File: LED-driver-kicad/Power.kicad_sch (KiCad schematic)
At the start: 32 parts, among them U1 LV2862XLVDDCR, U1 PD70210A, U3 LV2862XLVDDCR

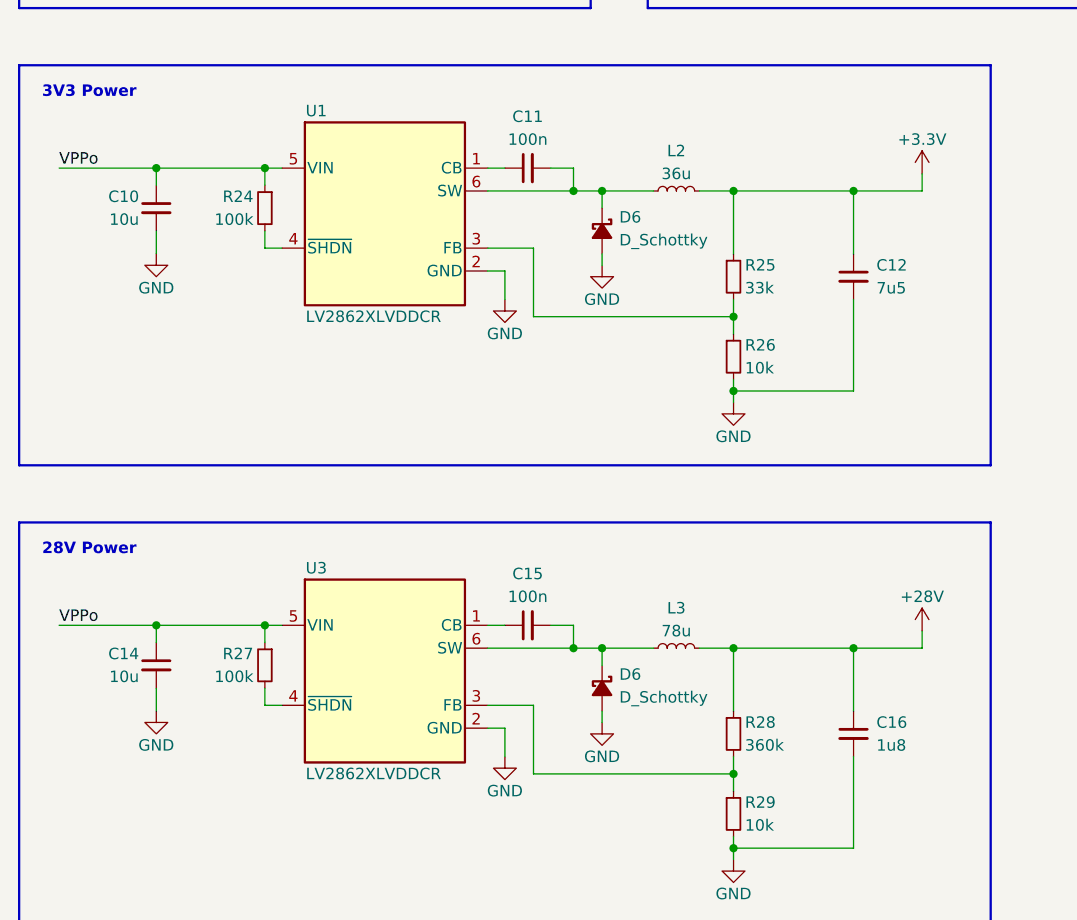
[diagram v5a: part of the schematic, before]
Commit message: update 3V3 power supply circuit
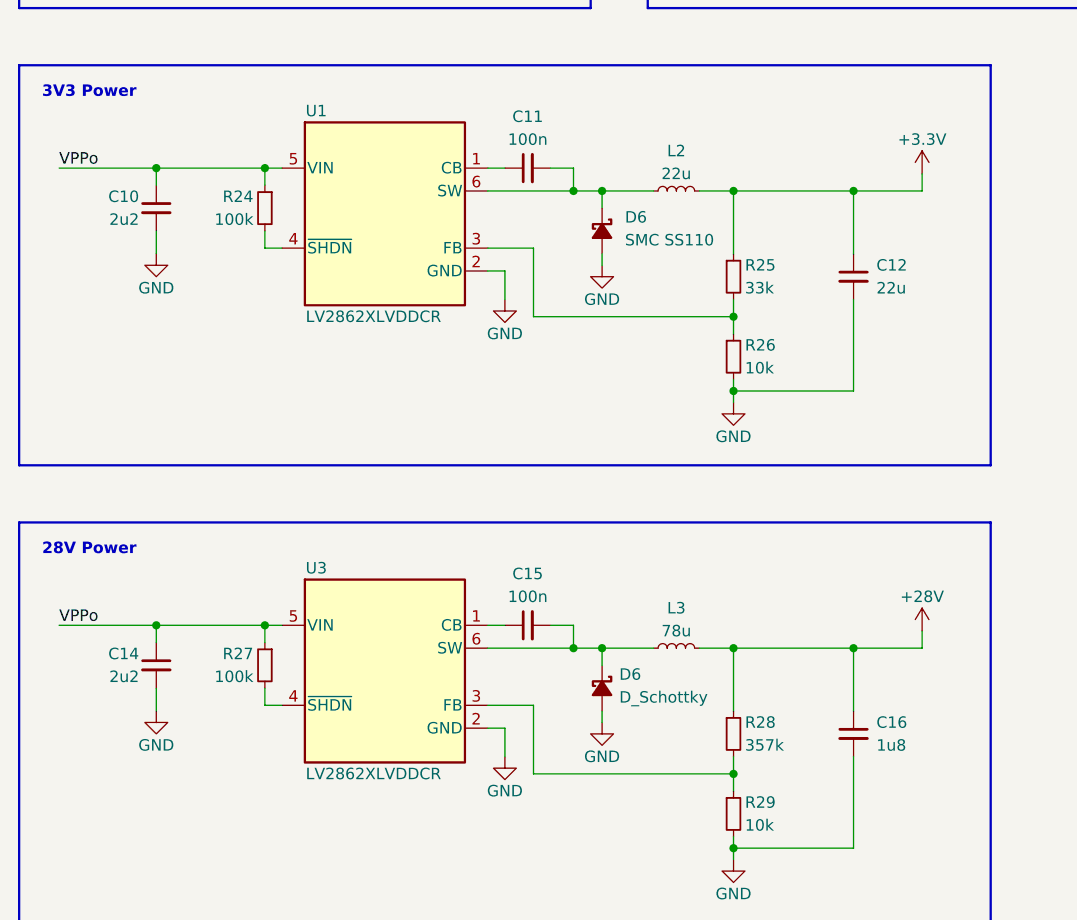
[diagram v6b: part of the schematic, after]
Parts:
- C10, C14: value 10u -> 2u2
- C12: value 7u5 -> 22u
- D6: value D_Schottky -> SMC SS110
- L2: value 36u -> 22u
- R28: value 360k -> 357k
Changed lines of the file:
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@@
       (effects (font (size 1.27 1.27)) (justify left))
     )
-    (property "Value" "7u5" (at 114.3 107.3213 0)
+    (property "Value" "22u" (at 114.3 107.3213 0)
       (effects (font (size 1.27 1.27)) (justify left))
     )
@@
       (effects (font (size 1.27 1.27)) (justify right))
     )
-    (property "Value" "10u" (at 32.385 150.495 0)
+    (property "Value" "2u2" (at 32.385 150.495 0)
       (effects (font (size 1.27 1.27)) (justify right))
     )
@@
   (symbol (lib_id "Device:D_Schottky_Small_Filled") (at 83.82 100.965 270) (unit 1)
     (in_bom yes) (on_board yes) (dnp no) (fields_autoplaced)
-    (property "Reference" "D6" (at 85.725 99.441 90)
-      (effects (font (size 1.27 1.27)) (justify left))
-    )
-    (property "Value" "D_Schottky" (at 85.725 101.981 90)
+    (property "Reference" "D6" (at 86.36 99.441 90)
+      (effects (font (size 1.27 1.27)) (justify left))
+    )
+    (property "Value" "SMC SS110" (at 86.36 101.981 90)
       (effects (font (size 1.27 1.27)) (justify left))
     )
@@
       (effects (font (size 1.27 1.27)))
     )
-    (property "Value" "36u" (at 92.075 94.615 90)
+    (property "Value" "22u" (at 92.075 94.615 90)
       (effects (font (size 1.27 1.27)))
     )
@@
       (effects (font (size 1.27 1.27)) (justify right))
     )
-    (property "Value" "10u" (at 32.385 99.695 0)
+    (property "Value" "2u2" (at 32.385 99.695 0)
       (effects (font (size 1.27 1.27)) (justify right))
     )
@@
       (effects (font (size 1.27 1.27)) (justify left))
     )
-    (property "Value" "360k" (at 99.695 158.115 0)
-      (effects (font (size 1.27 1.27)) (justify left))
-    )
+    (property "Value" "357k" (at 99.695 158.115 0)
+      (effects (font (size 1.27 1.27)) (justify left))
+    )

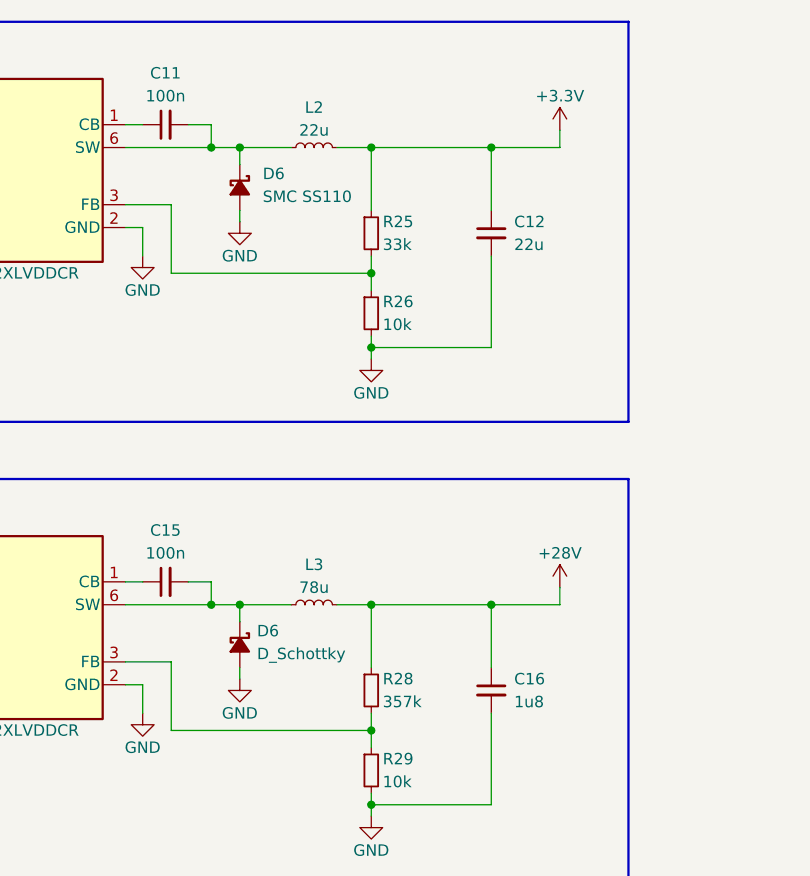
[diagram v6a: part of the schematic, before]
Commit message: update 28V power supply circuit
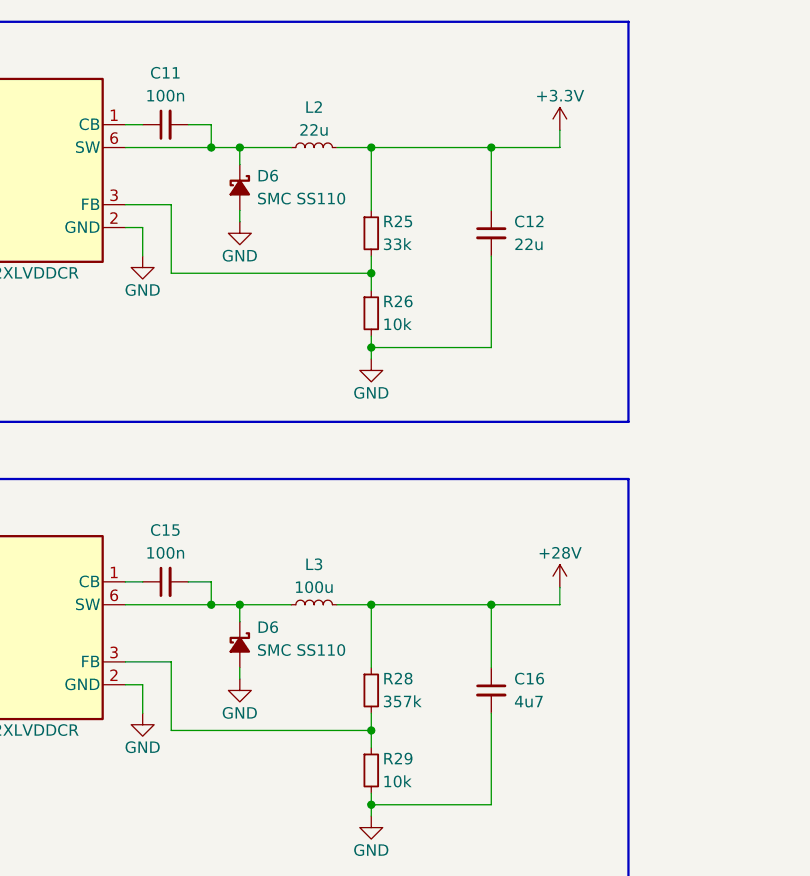
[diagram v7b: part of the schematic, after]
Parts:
- C16: value 1u8 -> 4u7
- D6: value D_Schottky -> SMC SS110
- L3: value 78u -> 100u
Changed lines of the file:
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@@
       (effects (font (size 1.27 1.27)))
     )
-    (property "Value" "78u" (at 92.075 145.415 90)
+    (property "Value" "100u" (at 92.075 145.415 90)
       (effects (font (size 1.27 1.27)))
     )
@@
       (effects (font (size 1.27 1.27)) (justify left))
     )
-    (property "Value" "1u8" (at 114.3 158.1213 0)
+    (property "Value" "4u7" (at 114.3 158.1213 0)
       (effects (font (size 1.27 1.27)) (justify left))
     )
@@
   )
   (symbol (lib_id "Device:D_Schottky_Small_Filled") (at 83.82 100.965 270) (unit 1)
-    (in_bom yes) (on_board yes) (dnp no) (fields_autoplaced)
-    (property "Reference" "D6" (at 86.36 99.441 90)
-      (effects (font (size 1.27 1.27)) (justify left))
-    )
-    (property "Value" "SMC SS110" (at 86.36 101.981 90)
+    (in_bom yes) (on_board yes) (dnp no)
+    (property "Reference" "D6" (at 85.725 99.695 90)
+      (effects (font (size 1.27 1.27)) (justify left))
+    )
+    (property "Value" "SMC SS110" (at 85.725 102.235 90)
       (effects (font (size 1.27 1.27)) (justify left))
     )
@@
   )
   (symbol (lib_id "Device:D_Schottky_Small_Filled") (at 83.82 151.765 270) (unit 1)
-    (in_bom yes) (on_board yes) (dnp no) (fields_autoplaced)
-    (property "Reference" "D6" (at 85.725 150.241 90)
-      (effects (font (size 1.27 1.27)) (justify left))
-    )
-    (property "Value" "D_Schottky" (at 85.725 152.781 90)
-      (effects (font (size 1.27 1.27)) (justify left))
-    )
+    (in_bom yes) (on_board yes) (dnp no)
+    (property "Reference" "D6" (at 85.725 149.86 90)
+      (effects (font (size 1.27 1.27)) (justify left))
+    )
+    (property "Value" "SMC SS110" (at 85.725 152.4 90)
+      (effects (font (size 1.27 1.27)) (justify left))
+    )

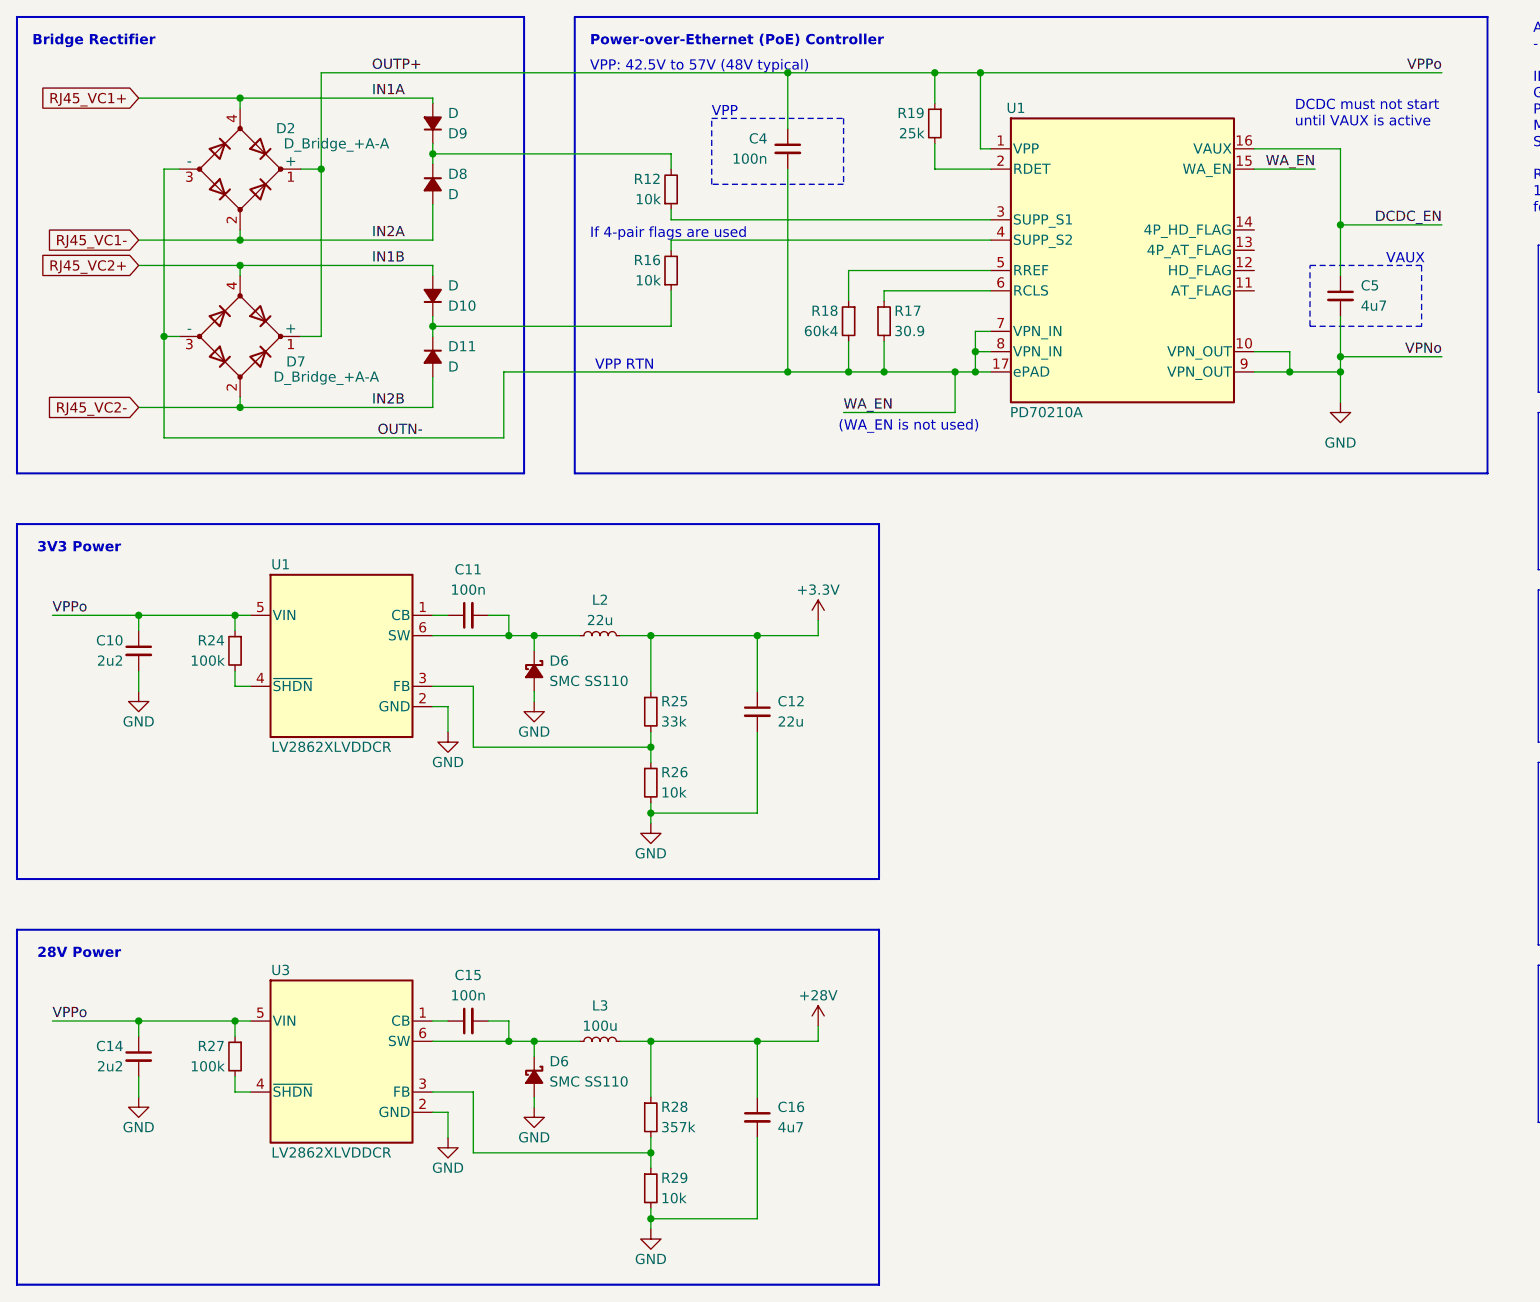
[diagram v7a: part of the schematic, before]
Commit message: update component designators
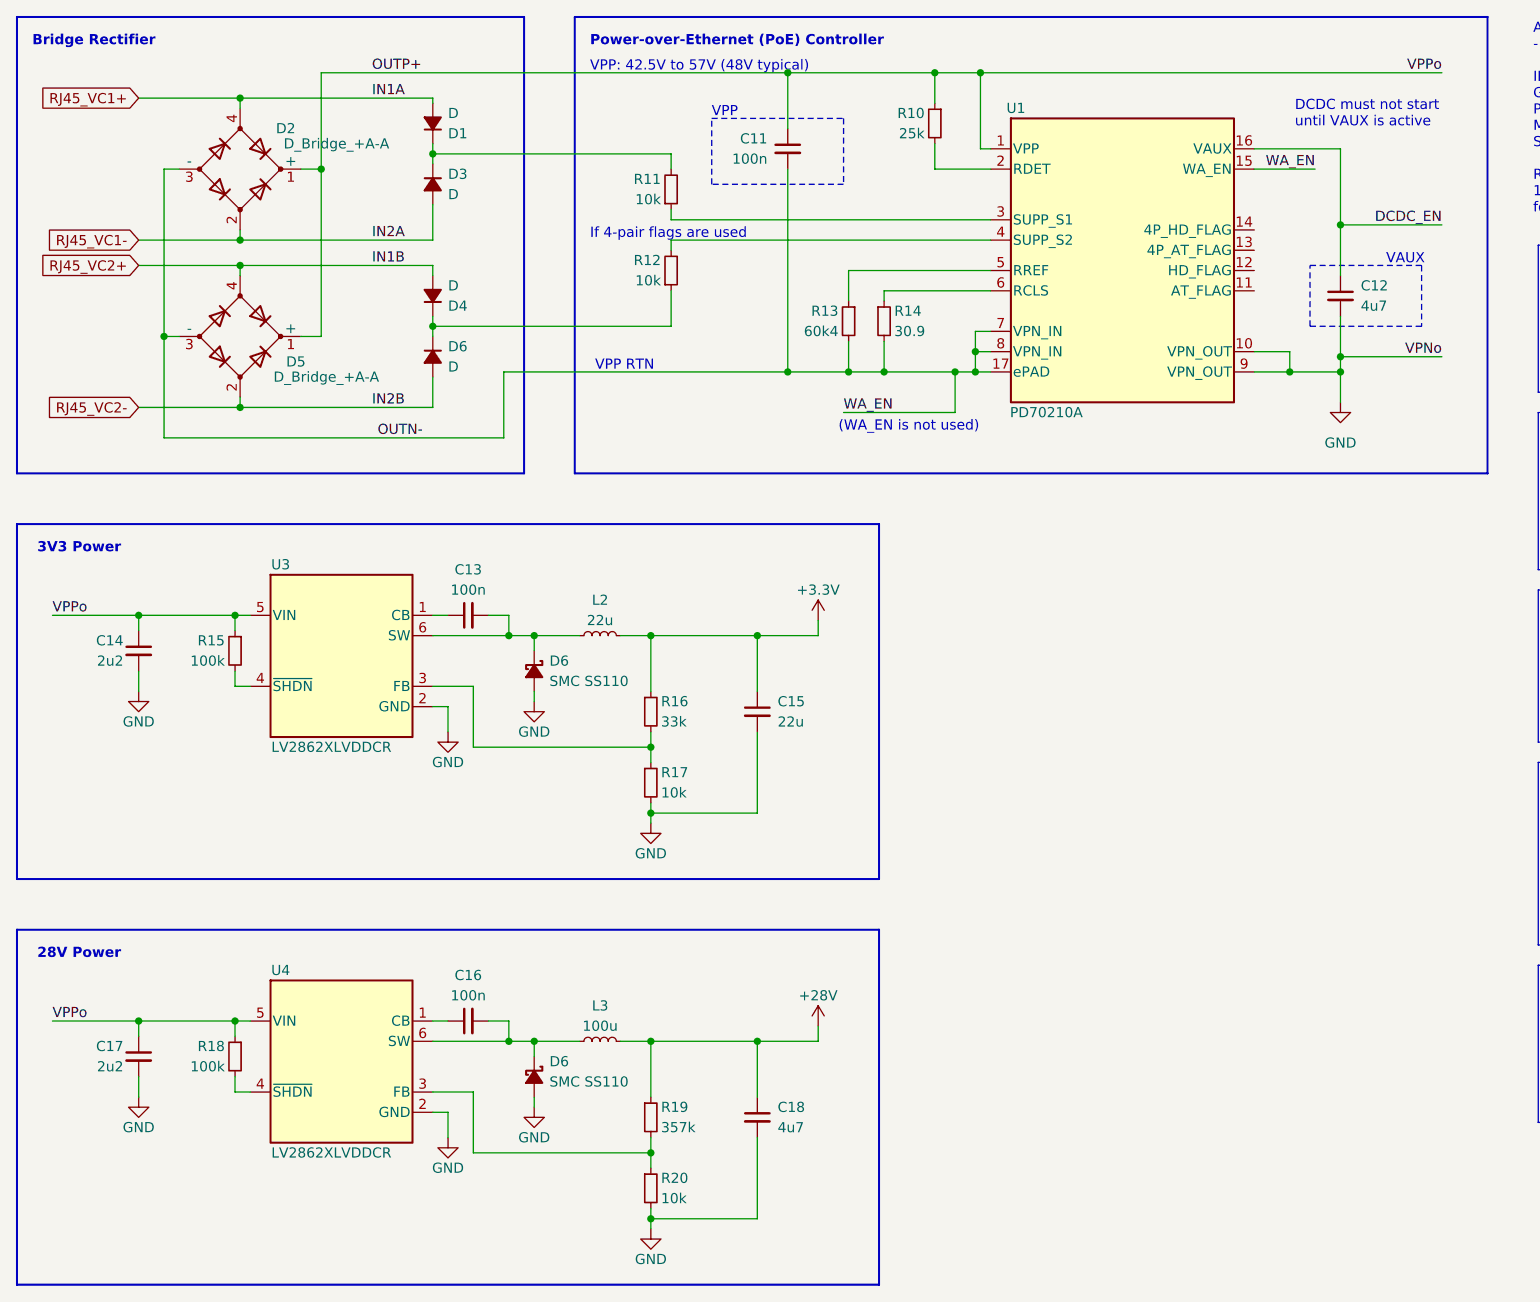
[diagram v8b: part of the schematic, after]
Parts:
- renumbered C4 to C11, C5 to C12, C11 to C13, C10 to C14, C12 to C15, C15 to C16, C14 to C17, C16 to C18, D9 to D1, D8 to D3, D10 to D4, D7 to D5, D11 to D6, R19 to R10, R12 to R11, R16 to R12, R18 to R13, R17 to R14, R24 to R15, R25 to R16, R26 to R17, R27 to R18, R28 to R19, R29 to R20, U1 to U3, U3 to U4
